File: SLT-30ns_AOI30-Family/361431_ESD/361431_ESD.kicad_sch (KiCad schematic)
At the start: 9 parts, among them U1 16-Pin_SLx_Can

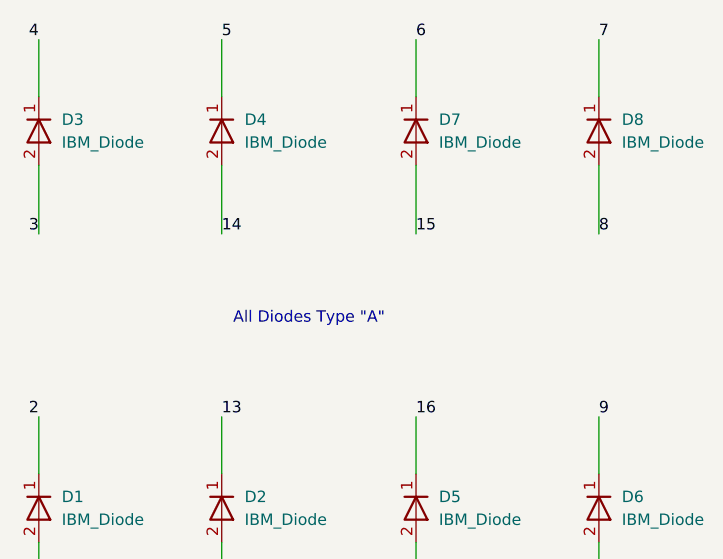
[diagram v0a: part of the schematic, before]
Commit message: Update schematic pdfs
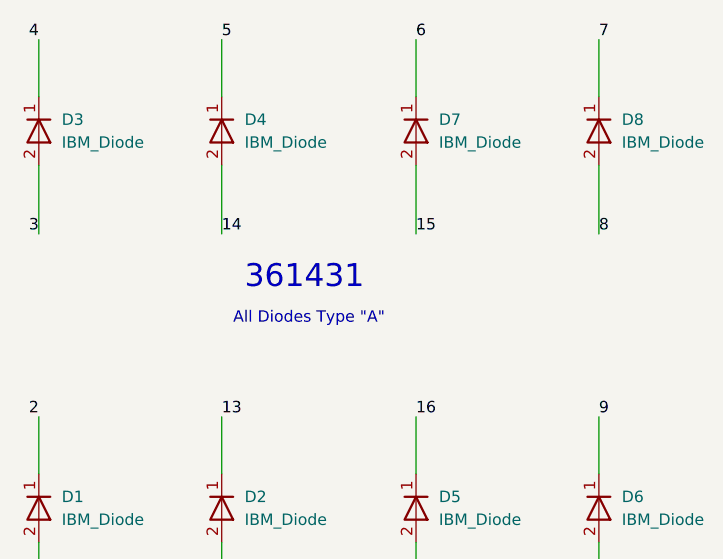
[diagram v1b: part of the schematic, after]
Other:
- note added: "361431"
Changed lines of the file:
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@@
     (effects (font (size 1.27 1.27)) (justify left bottom))
+  )
+  (text "361431" (at 110.49 92.71 0)
+    (effects (font (size 2.54 2.54)) (justify left bottom))
   )
   (label "15" (at 129.54 86.36 0)
